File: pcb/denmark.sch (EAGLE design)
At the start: 101 parts, among them IC1 74AHC1G32DBV, IC2 REG1117, Q1 8.0 MHz, U2 MB85RCSOIC8, X1 22-23-2021, X2 22-23-2031, X3 22-23-2051, X4 22-23-2021

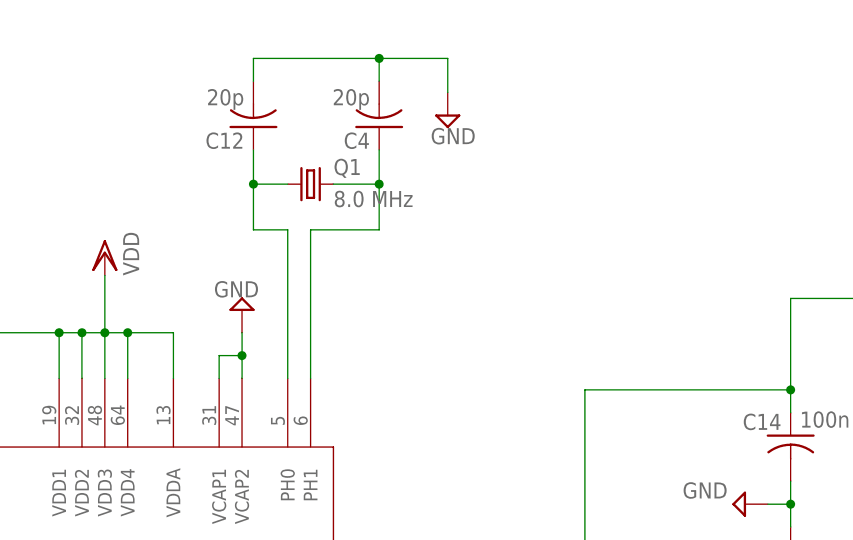
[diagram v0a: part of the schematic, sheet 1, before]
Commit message: More BOM and schematic cleanup
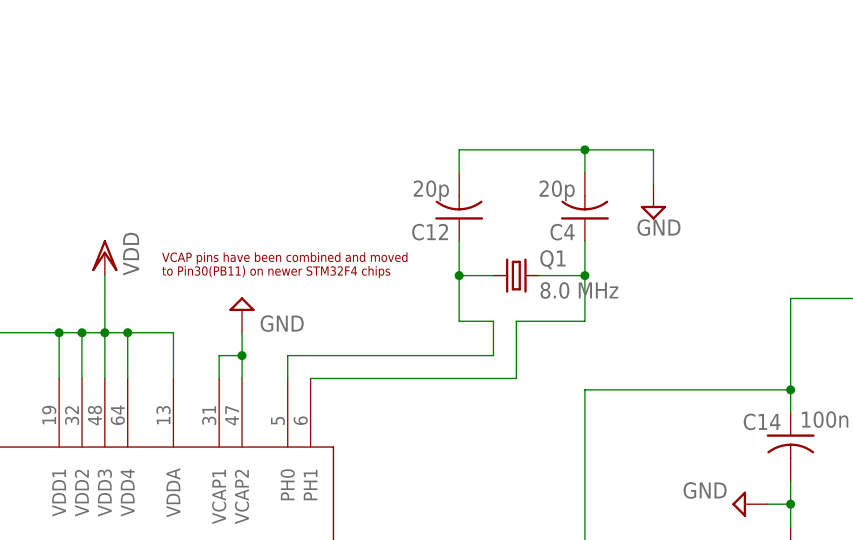
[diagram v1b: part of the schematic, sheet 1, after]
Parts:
- renumbered U$1 to U1
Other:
- note added: "VCAP pins have been combined and moved to Pin30(PB11) on newer STM32F4 chips"
- moved on the sheet: C12, C4, Q1
